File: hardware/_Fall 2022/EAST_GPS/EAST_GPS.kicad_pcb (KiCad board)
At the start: 2 copper layers, 76.2 x 66.7 mm, 4 parts, among them J1 Conn_02x09_Odd_Even, U1 GPS-14414, U2 RFM69HCW_Breakout

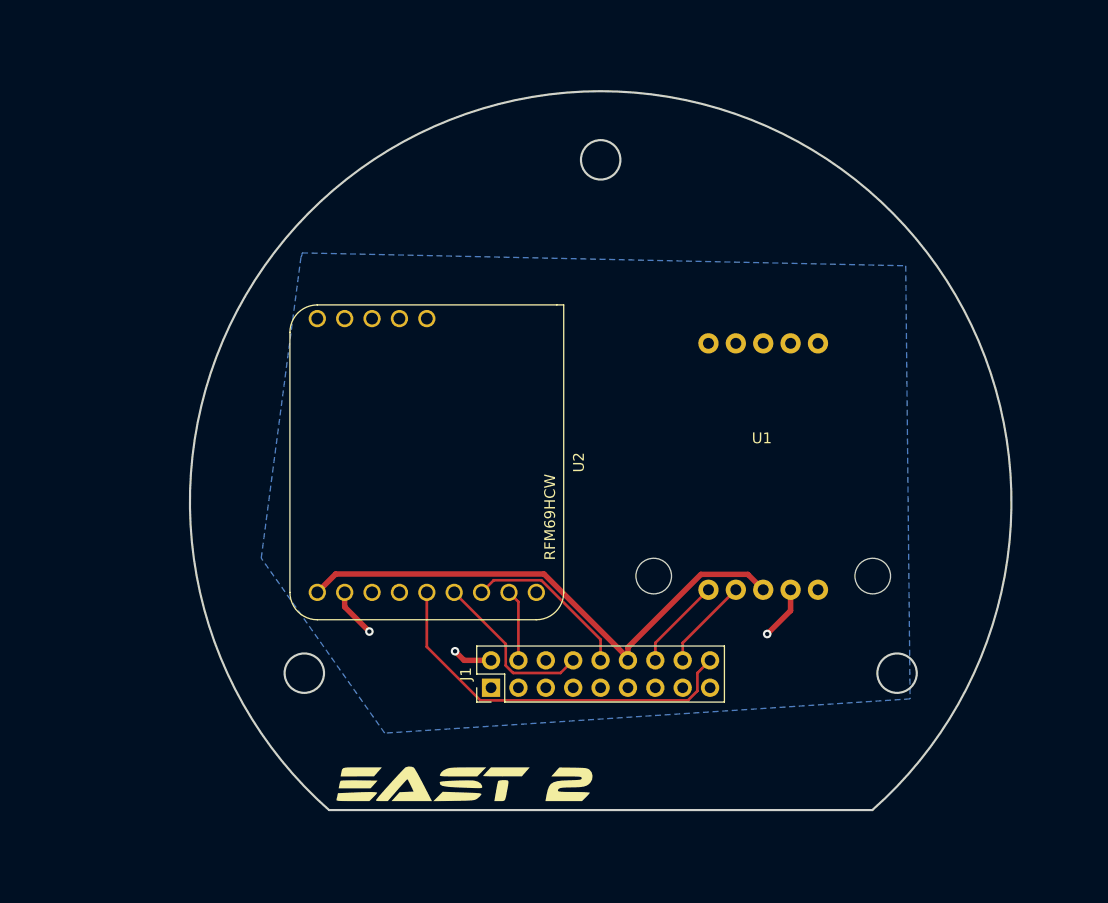
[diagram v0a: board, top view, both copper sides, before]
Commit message: add plated holes to both east boards
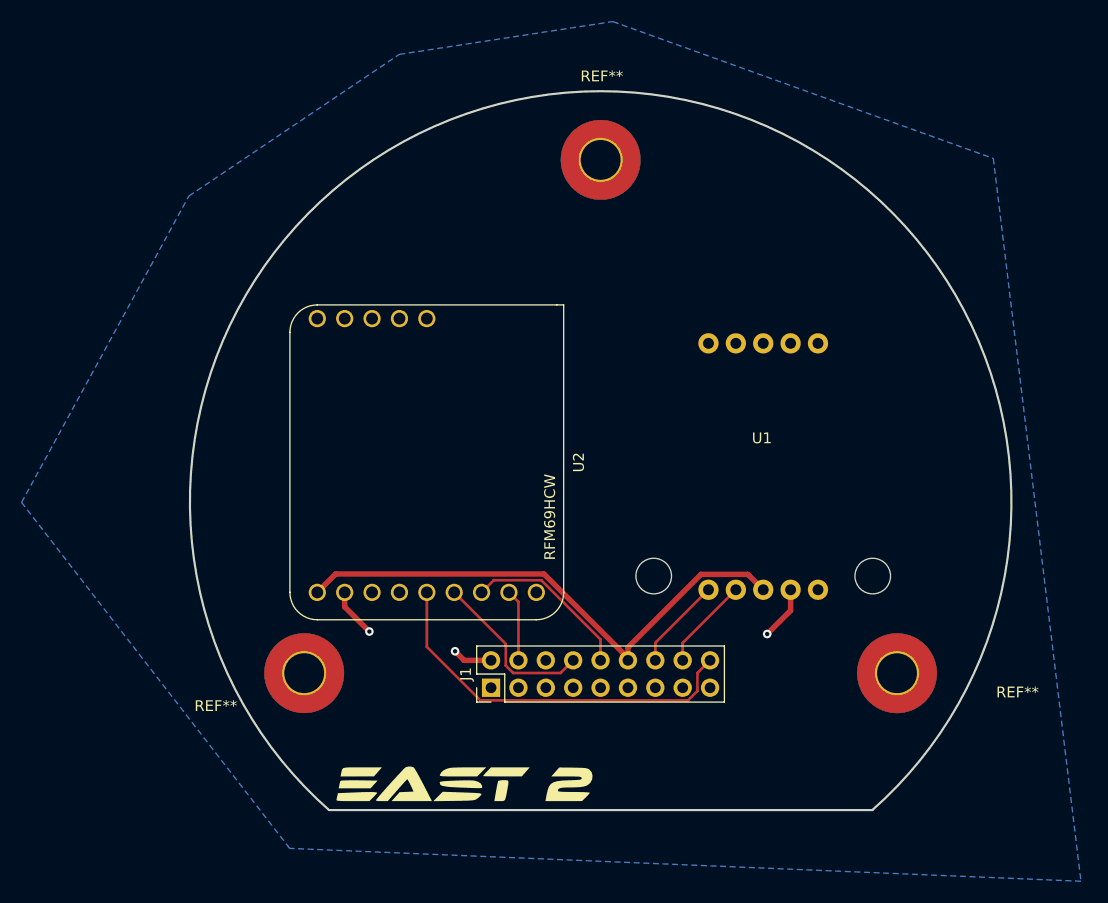
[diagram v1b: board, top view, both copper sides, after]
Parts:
- added REF**: MountingHole_3.7mm_Pad_TopBottom, MountingHole:MountingHole_3.7mm_Pad_TopBottom, F.Cu at (170.6, 116.8)
- added REF**: MountingHole_3.7mm_Pad_TopBottom, MountingHole:MountingHole_3.7mm_Pad_TopBottom, F.Cu at (115.6, 116.8)
- added REF**: MountingHole_3.7mm_Pad_TopBottom, MountingHole:MountingHole_3.7mm_Pad_TopBottom, F.Cu at (143.1, 69.2)
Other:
- outline, holes or cut-outs redrawn
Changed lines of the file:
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@@
   (net 31 "/V_BATT")
   (net 32 "/CS 4")
+  (footprint "MountingHole:MountingHole_3.7mm_Pad_TopBottom" (layer "F.Cu")
+    (at 170.641661 116.84528)
+    (descr "Mounting Hole 3.7mm")
+    (tags "mounting hole 3.7mm")
+    (attr exclude_from_pos_files exclude_from_bom)
+    (fp_text reference "REF**" (at 11.176 1.778) (layer "F.SilkS")
+      (effects (font (size 1 1) (thickness 0.15)))
+    )
+    (fp_text value "MountingHole_3.7mm_Pad_TopBottom" (at 0 4.7) (layer "F.Fab")
+      (effects (font (size 1 1) (thickness 0.15)))
+    )
+    (fp_text user "${REFERENCE}" (at 0 0) (layer "F.Fab")
+      (effects (font (size 1 1) (thickness 0.15)))
+    )
+    (fp_circle (center 0 0) (end 3.7 0) (layer "Cmts.User") (width 0.15) (fill none))
+    (fp_circle (center 0 0) (end 3.95 0) (layer "F.CrtYd") (width 0.05) (fill none))
+    (pad "1" thru_hole circle (at 0 0) (size 4.1 4.1) (drill 3.7) (layers *.Cu *.Mask))
+    (pad "1" connect circle (at 0 0) (size 7.4 7.4) (layers "F.Cu" "F.Mask"))
+    (pad "1" connect circle (at 0 0) (size 7.4 7.4) (layers "B.Cu" "B.Mask"))
+  )
   (footprint "LOGO" (layer "F.Cu")
     (at 130.376838 127.354926)
@@
     (fp_circle (center 10.033 -10.287) (end 12.827 -10.287) (layer "F.CrtYd") (width 0.127) (fill none))
     (pad "" np_thru_hole circle (at -10.287 -10.287 180) (size 3.302 3.302) (drill 3.302) (layers F&B.Cu *.Mask))
-    (pad "" np_thru_hole circle (at 10.033 -10.287 180) (size 3.302 3.302) (drill 3.302) (layers *.Cu *.Mask))
+    (pad "" np_thru_hole circle (at 10.033 -10.287 180) (size 3.302 3.302) (drill 3.302) (layers F&B.Cu *.Mask))
     (pad "1" thru_hole circle (at -5.207 -11.557 270) (size 1.8796 1.8796) (drill 1.016) (layers *.Cu *.Mask)
       (net 25 "unconnected-(U1-Pad1)") (pinfunction "INT") (pintype "output+no_connect") (solder_mask_margin 0.1016))
@@
     )
   )
-  (gr_circle (center 143.150419 69.216397) (end 141.321619 69.216397) (layer "Dwgs.User") (width 0.2) (fill none))
+  (footprint "MountingHole:MountingHole_3.7mm_Pad_TopBottom" (layer "F.Cu")
+    (at 115.644369 116.84)
+    (descr "Mounting Hole 3.7mm")
+    (tags "mounting hole 3.7mm")
+    (attr exclude_from_pos_files exclude_from_bom)
+    (fp_text reference "REF**" (at -8.202369 3.048) (layer "F.SilkS")
+      (effects (font (size 1 1) (thickness 0.15)))
+    )
+    (fp_text value "MountingHole_3.7mm_Pad_TopBottom" (at 0 4.7) (layer "F.Fab")
+      (effects (font (size 1 1) (thickness 0.15)))
+    )
+    (fp_text user "${REFERENCE}" (at 0 0) (layer "F.Fab")
+      (effects (font (size 1 1) (thickness 0.15)))
+    )
+    (fp_circle (center 0 0) (end 3.7 0) (layer "Cmts.User") (width 0.15) (fill none))
+    (fp_circle (center 0 0) (end 3.95 0) (layer "F.CrtYd") (width 0.05) (fill none))
+    (pad "1" thru_hole circle (at 0 0) (size 4.1 4.1) (drill 3.7) (layers *.Cu *.Mask))
+    (pad "1" connect circle (at 0 0) (size 7.4 7.4) (layers "F.Cu" "F.Mask"))
+    (pad "1" connect circle (at 0 0) (size 7.4 7.4) (layers "B.Cu" "B.Mask"))
+  )
+  (footprint "MountingHole:MountingHole_3.7mm_Pad_TopBottom" (layer "F.Cu")
+    (at 143.147778 69.222624)
+    (descr "Mounting Hole 3.7mm")
+    (tags "mounting hole 3.7mm")
+    (attr exclude_from_pos_files exclude_from_bom)
+    (fp_text reference "REF**" (at 0.108222 -7.754624) (layer "F.SilkS")
+      (effects (font (size 1 1) (thickness 0.15)))
+    )
+    (fp_text value "MountingHole_3.7mm_Pad_TopBottom" (at 0 4.7) (layer "F.Fab")
+      (effects (font (size 1 1) (thickness 0.15)))
+    )
+    (fp_text user "${REFERENCE}" (at 0 0) (layer "F.Fab")
+      (effects (font (size 1 1) (thickness 0.15)))
+    )
+    (fp_circle (center 0 0) (end 3.7 0) (layer "Cmts.User") (width 0.15) (fill none))
+    (fp_circle (center 0 0) (end 3.95 0) (layer "F.CrtYd") (width 0.05) (fill none))
+    (pad "1" connect circle (at 0 0) (size 7.4 7.4) (layers "F.Cu" "F.Mask"))
+    (pad "1" connect circle (at 0 0) (size 7.4 7.4) (layers "B.Cu" "B.Mask"))
+    (pad "1" thru_hole circle (at 0 0) (size 4.1 4.1) (drill 3.7) (layers *.Cu *.Mask))
+  )
+  (gr_circle (center 143.150419 69.216397) (end 144.979219 69.216397) (layer "Dwgs.User") (width 0.2) (fill none))
+  (gr_circle (center 170.645919 116.84) (end 172.474719 116.84) (layer "Dwgs.User") (width 0.2) (fill none))
   (gr_line (start 131.720419 114.300466) (end 154.580419 114.300466) (layer "Dwgs.User") (width 0.2))
+  (gr_circle (center 115.654919 116.84) (end 117.483719 116.84) (layer "Dwgs.User") (width 0.2) (fill none))
   (gr_line (start 154.580419 119.380466) (end 131.720419 119.380466) (layer "Dwgs.User") (width 0.2))
-  (gr_circle (center 115.654919 116.84) (end 113.826119 116.84) (layer "Dwgs.User") (width 0.2) (fill none))
-  (gr_arc (start 117.949638 129.540466) (mid 143.150419 62.865466) (end 168.3512 129.540466) (layer "Dwgs.User") (width 0.2))
-  (gr_circle (center 170.645919 116.84) (end 168.817119 116.84) (layer "Dwgs.User") (width 0.2) (fill none))
   (gr_line (start 131.720419 119.380466) (end 131.720419 114.300466) (layer "Dwgs.User") (width 0.2))
-  (gr_line (start 117.949638 129.540466) (end 168.3512 129.540466) (layer "Dwgs.User") (width 0.2))
   (gr_line (start 154.580419 114.300466) (end 154.580419 119.380466) (layer "Dwgs.User") (width 0.2))
   (gr_line (start 117.949638 129.540466) (end 168.3512 129.540466) (layer "Edge.Cuts") (width 0.2))
-  (gr_circle (center 143.150419 69.216397) (end 144.979219 69.216397) (layer "Edge.Cuts") (width 0.2) (fill none))
-  (gr_circle (center 170.645919 116.84) (end 172.474719 116.84) (layer "Edge.Cuts") (width 0.2) (fill none))
   (gr_arc (start 117.949638 129.540466) (mid 143.150419 62.848534) (end 168.3512 129.540466) (layer "Edge.Cuts") (width 0.2))
-  (gr_circle (center 115.654919 116.84) (end 117.483719 116.84) (layer "Edge.Cuts") (width 0.2) (fill none))
   (segment (start 130.4848 115.6512) (end 129.6416 114.808) (width 0.508) (layer "F.Cu") (net 1))
   (segment (start 119.4 110.6878) (end 121.6914 112.9792) (width 0.508) (layer "F.Cu") (net 1))
@@
   (segment (start 148.219 115.6512) (end 148.219 114.03245) (width 0.25) (layer "F.Cu") (net 14))
   (zone (net 1) (net_name "/GND") (layer "B.Cu") (hatch edge 0.508)
-    (connect_pads (clearance 0.508))
+    (connect_pads (clearance 1))
     (min_thickness 0.254) (filled_areas_thickness no)
     (fill yes (thermal_gap 0.508) (thermal_bridge_width 0.508))
     (polygon
       (pts
-        (xy 171.45 79.0448)
-        (xy 171.8564 119.2276)
-        (xy 123.1138 122.4026)
-        (xy 111.6584 106.172)
-        (xy 115.3414 78.2574)
-        (xy 115.443 78.0542)
-        (xy 115.443 77.851)
+        (xy 179.578 69.088)
+        (xy 187.706 136.144)
+        (xy 114.3 133.096)
+        (xy 89.422414 101.001584)
+        (xy 104.941814 72.578984)
+        (xy 124.46 59.436)
+        (xy 144.272 56.388)
       )
     )
@@
       12d6c219-1b6c-4472-9cfd-8704c5a4d38e
       1bad86d5-b5fa-427a-9390-144a8bae3194
-      3781492c-401b-4b53-9f38-69314c1be3f5
       3ca255fb-cb87-41ac-82dd-7204822815a6
       5757b1d2-8f9f-41f1-9085-d77ea9422919
@@
       cda0e2c0-0b07-46a9-b8b1-380b8da2df3c
       e3435ebd-4131-4f47-a389-2980d55a0016
-      e6fe229e-2151-4404-9210-35be1228e68d
       e8a13ea9-6b8c-43aa-a840-b2450a445a94
     )

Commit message: change board 4 C size and GPS labels hided
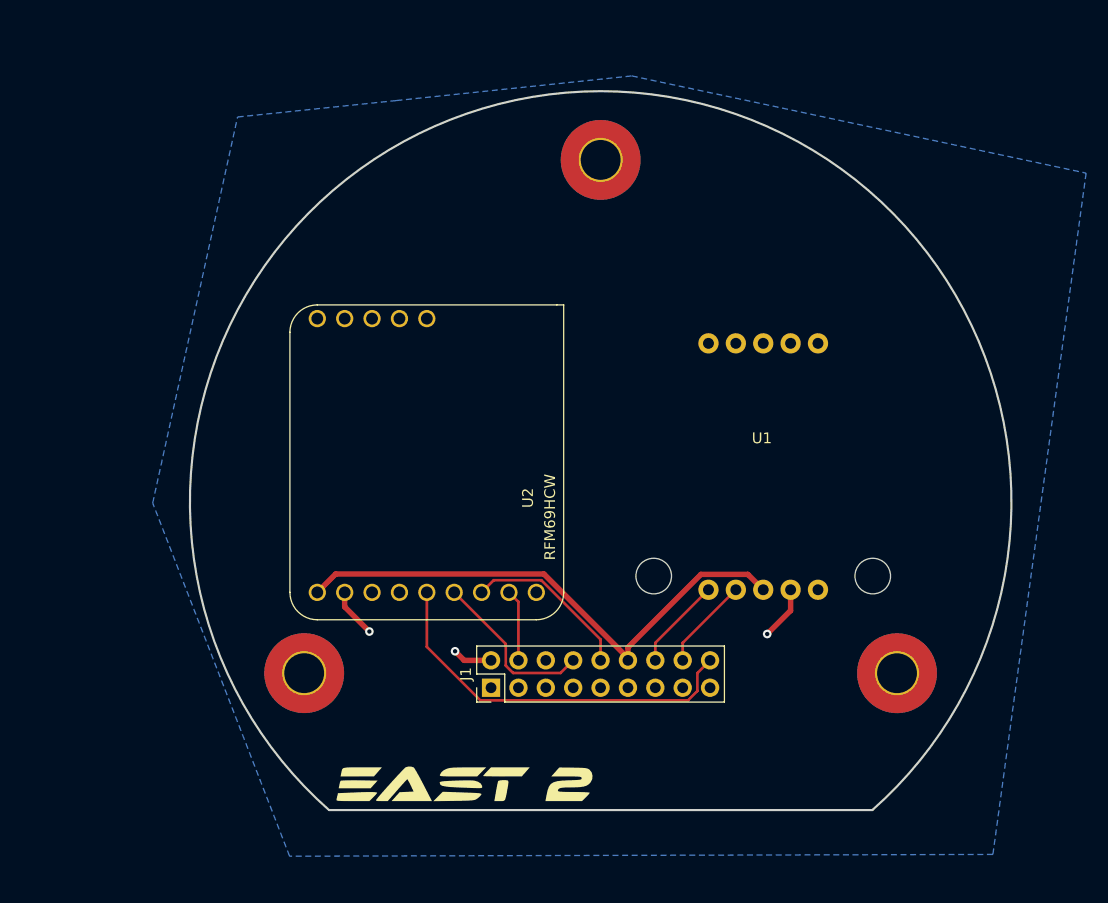
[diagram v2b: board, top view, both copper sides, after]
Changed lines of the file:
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@@
     (tags "mounting hole 3.7mm")
     (attr exclude_from_pos_files exclude_from_bom)
-    (fp_text reference "REF**" (at 11.176 1.778) (layer "F.SilkS")
-      (effects (font (size 1 1) (thickness 0.15)))
-    )
-    (fp_text value "MountingHole_3.7mm_Pad_TopBottom" (at 0 4.7) (layer "F.Fab")
+    (fp_text reference "REF**" (at 11.176 1.778) (layer "F.SilkS") hide
+      (effects (font (size 1 1) (thickness 0.15)))
+    )
+    (fp_text value "MountingHole_3.7mm_Pad_TopBottom" (at 0 4.7) (layer "F.Fab") hide
       (effects (font (size 1 1) (thickness 0.15)))
     )
@@
     (property "Sheetname" "")
     (attr through_hole)
-    (fp_text reference "U2" (at 0 -14.105 90) (layer "F.SilkS")
+    (fp_text reference "U2" (at 3.304 -9.378 -90) (layer "F.SilkS")
       (effects (font (size 1 1) (thickness 0.15)))
     )
@@
       (effects (font (size 1 1) (thickness 0.15)))
     )
-    (fp_text value "Conn_02x09_Odd_Even" (at 1.27 22.65 90) (layer "F.Fab")
+    (fp_text value "Conn_02x09_Odd_Even" (at 1.27 22.65 90) (layer "F.Fab") hide
       (effects (font (size 1 1) (thickness 0.15)))
     )
@@
     (tags "mounting hole 3.7mm")
     (attr exclude_from_pos_files exclude_from_bom)
-    (fp_text reference "REF**" (at -8.202369 3.048) (layer "F.SilkS")
-      (effects (font (size 1 1) (thickness 0.15)))
-    )
-    (fp_text value "MountingHole_3.7mm_Pad_TopBottom" (at 0 4.7) (layer "F.Fab")
+    (fp_text reference "REF**" (at -8.202369 3.048) (layer "F.SilkS") hide
+      (effects (font (size 1 1) (thickness 0.15)))
+    )
+    (fp_text value "MountingHole_3.7mm_Pad_TopBottom" (at 0 4.7) (layer "F.Fab") hide
       (effects (font (size 1 1) (thickness 0.15)))
     )
@@
     (tags "mounting hole 3.7mm")
     (attr exclude_from_pos_files exclude_from_bom)
-    (fp_text reference "REF**" (at 0.108222 -7.754624) (layer "F.SilkS")
-      (effects (font (size 1 1) (thickness 0.15)))
-    )
-    (fp_text value "MountingHole_3.7mm_Pad_TopBottom" (at 0 4.7) (layer "F.Fab")
+    (fp_text reference "REF**" (at 0.108222 -7.754624) (layer "F.SilkS") hide
+      (effects (font (size 1 1) (thickness 0.15)))
+    )
+    (fp_text value "MountingHole_3.7mm_Pad_TopBottom" (at 0 4.7) (layer "F.Fab") hide
       (effects (font (size 1 1) (thickness 0.15)))
     )
@@
     (polygon
       (pts
-        (xy 179.578 69.088)
-        (xy 187.706 136.144)
-        (xy 114.3 133.096)
-        (xy 89.422414 101.001584)
-        (xy 104.941814 72.578984)
-        (xy 124.46 59.436)
-        (xy 144.272 56.388)
+        (xy 188.183859 70.447323)
+        (xy 179.537518 133.656545)
+        (xy 114.289659 133.821222)
+        (xy 101.589659 101.055222)
+        (xy 109.463659 65.241222)
+        (xy 124.195659 63.717222)
+        (xy 146.039659 61.431222)
       )
     )
@@
       1285237e-3b77-40e5-80f7-0f0e5d174dc9
       12d6c219-1b6c-4472-9cfd-8704c5a4d38e
-      1bad86d5-b5fa-427a-9390-144a8bae3194
       3ca255fb-cb87-41ac-82dd-7204822815a6
       5757b1d2-8f9f-41f1-9085-d77ea9422919
       62e84dc7-3e37-439d-80c2-cb356d97d02e
-      85980339-9dba-4007-abd9-6ce50e26be95
       9f998e7b-41bd-4c90-88a7-a4af32856d60
-      cda0e2c0-0b07-46a9-b8b1-380b8da2df3c
       e3435ebd-4131-4f47-a389-2980d55a0016
       e8a13ea9-6b8c-43aa-a840-b2450a445a94

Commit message: minor fixes
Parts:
- moved ? 0.36 mm to (130.1, 127.2)
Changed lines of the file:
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@@
   )
   (footprint "LOGO" (layer "F.Cu")
-    (at 130.376838 127.354926)
+    (at 130.05796 127.184274)
     (attr board_only exclude_from_pos_files exclude_from_bom)
     (fp_text reference "" (at 0 0) (layer "F.SilkS")
